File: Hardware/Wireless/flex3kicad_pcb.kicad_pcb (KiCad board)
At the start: 2 copper layers, 19 x 49.9 mm, 2 parts

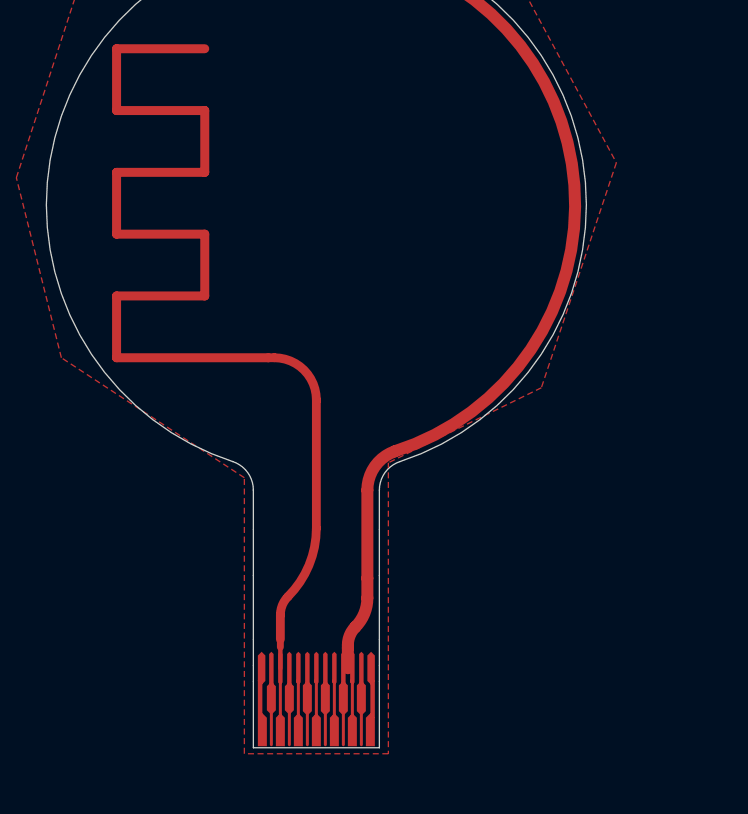
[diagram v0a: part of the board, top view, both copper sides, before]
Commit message: added status led
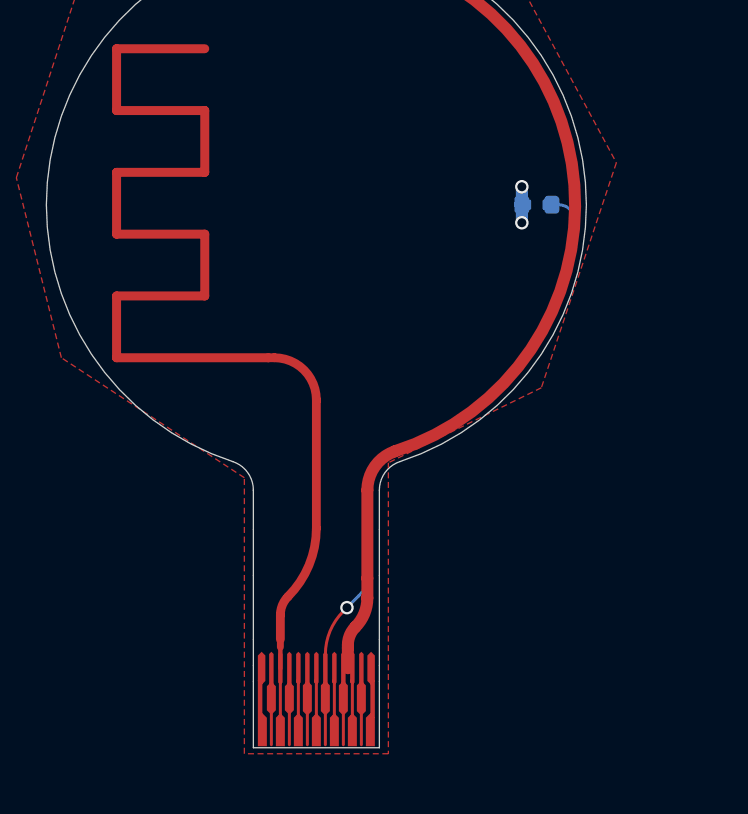
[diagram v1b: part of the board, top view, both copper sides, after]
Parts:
- added D1: BLUE, Library:0402, B.Cu at (185.2, 75.9)
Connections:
- REF** pad 8: (no net) -> led
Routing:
- net led: track 0.00 -> 7.54 mm, vias 0 -> 1
- net gnd: track 0.00 -> 1.20 mm, vias 0 -> 2

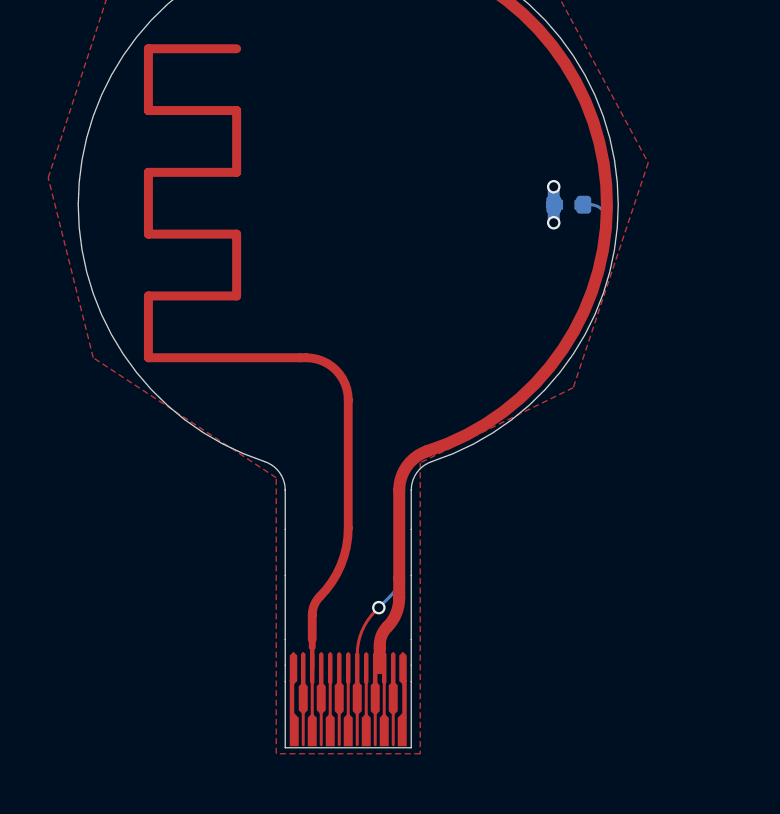
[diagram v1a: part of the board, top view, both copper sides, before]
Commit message: revolute production boards
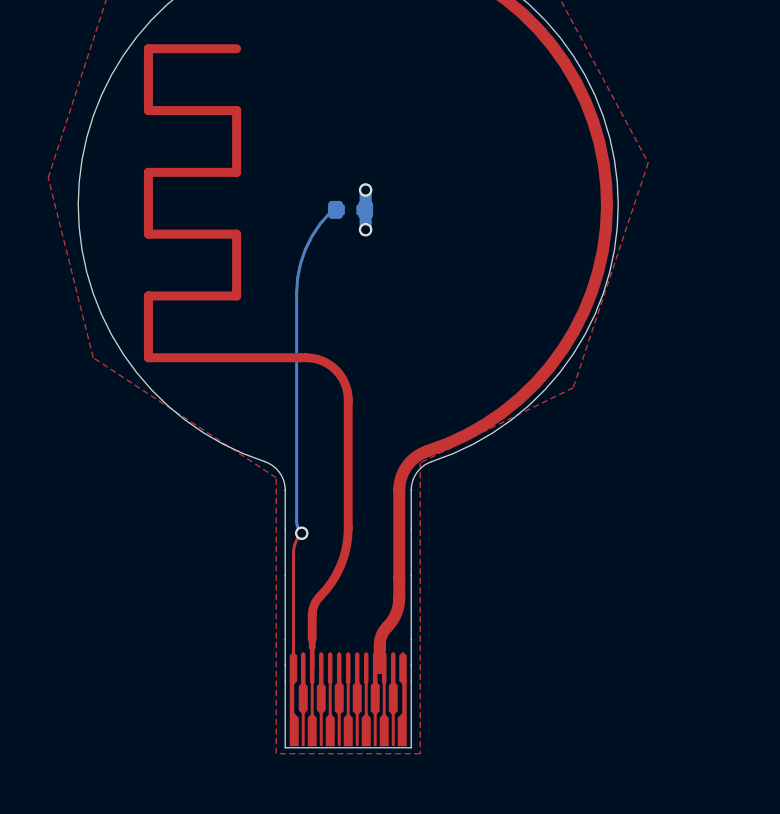
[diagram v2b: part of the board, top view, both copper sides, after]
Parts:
- moved D1 7.27 mm to (178.0, 76.1), turned to 0 degrees
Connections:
- REF** pad 1: gnd -> led
- REF** pad 8: led -> (no net)
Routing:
- net led: track 7.54 -> 15.6 mm

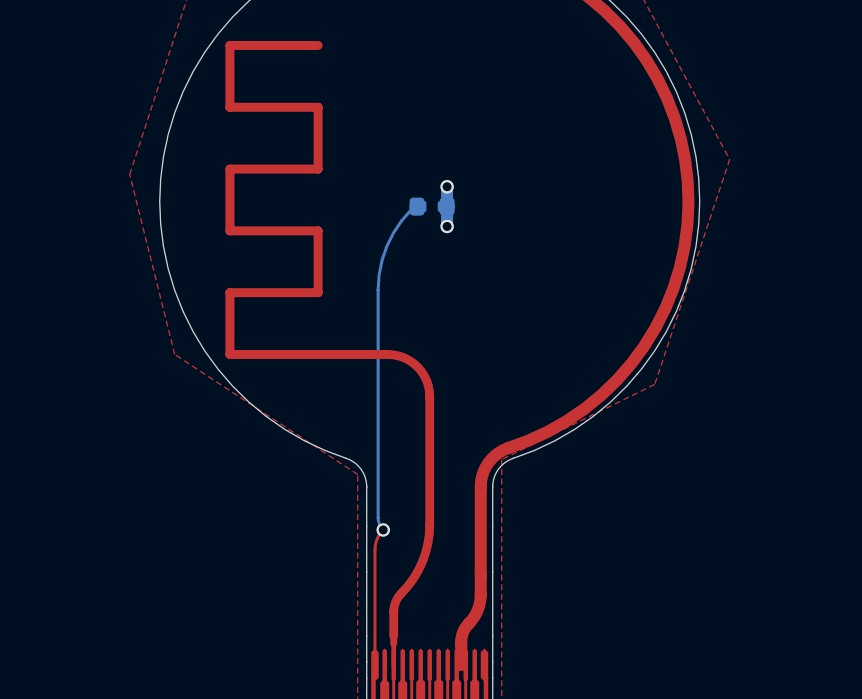
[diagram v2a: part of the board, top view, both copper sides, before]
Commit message: centered flex pcb, made pcb 1.6mm
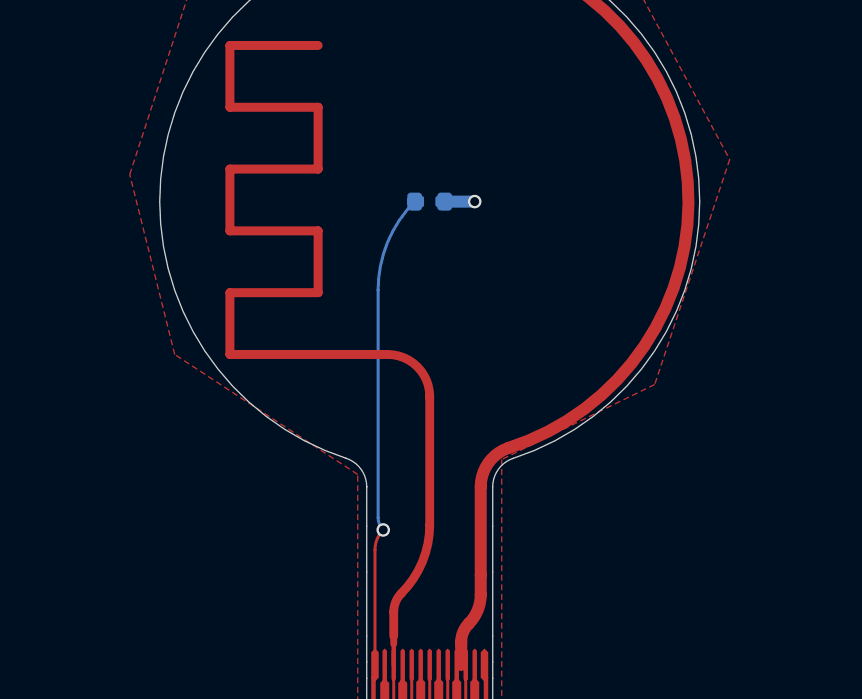
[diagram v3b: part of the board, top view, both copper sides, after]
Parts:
- moved D1 0.19 mm to (177.9, 75.9)
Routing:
- net gnd: track 1.32 -> 1.00 mm, vias 2 -> 1
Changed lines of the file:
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@@
 		(allow_soldermask_bridges_in_footprints no)
 		(aux_axis_origin 171 95)
-		(grid_origin 177.9791 76.0709)
+		(grid_origin 177.89999 75.903507)
 		(pcbplotparams
 			(layerselection 0x00410fc_ffffffff)
@@
 			(drillshape 0)
 			(scaleselection 1)
-			(outputdirectory "../../../../../../../../Desktop/RevoluteJanurary/Flex/")
+			(outputdirectory "../../../gerberflex/")
 		)
 	)
@@
 	(footprint "Library:0402"
 		(layer "B.Cu")
-		(at 177.9791 76.0709)
+		(at 177.89999 75.903507)
 		(property "Reference" "D1"
 			(at 0.040001 1.829998 180)
@@
 	)
 	(gr_arc
-		(start 175.499106 84.670778)
-		(mid 169.028778 76.0709)
-		(end 175.499106 67.471022)
+		(start 175.419996 84.503385)
+		(mid 168.949668 75.903507)
+		(end 175.419996 67.303629)
 		(stroke
 			(width 0.1)
@@
 		(layer "User.1")
 	)
-	(gr_arc
-		(start 175.698594 84.55781)
-		(mid 169.191364 76.134519)
-		(end 175.575958 67.617897)
+	(gr_line
+		(start 175.240886 62.24302)
+		(end 180.559114 62.24302)
+		(stroke
+			(width 1)
+			(type default)
+		)
+		(layer "User.1")
+	)
+	(gr_arc
+		(start 175.619484 84.390417)
+		(mid 169.112254 75.967126)
+		(end 175.496848 67.450504)
 		(stroke
 			(width 0.3)
@@
 	)
 	(gr_circle
-		(center 177.9791 76.0709)
-		(end 182.821644 76.083633)
+		(center 177.89999 75.903507)
+		(end 182.742534 75.91624)
 		(stroke
 			(width 7.5)
@@
 	)
 	(gr_line
-		(start 175.499106 84.670778)
-		(end 180.459094 84.670778)
+		(start 175.419996 84.503385)
+		(end 180.379984 84.503385)
 		(stroke
 			(width 0.1)
@@
 	)
 	(gr_arc
-		(start 180.278254 67.576361)
-		(mid 186.77911 76.015206)
-		(end 180.385585 84.535656)
+		(start 180.199144 67.408968)
+		(mid 186.700001 75.847814)
+		(end 180.306475 84.368263)
 		(stroke
 			(width 0.3)
@@
 	)
 	(gr_arc
-		(start 177.086246 84.556508)
-		(mid 169.446795 76.121011)
-		(end 176.986638 67.596364)
+		(start 177.007136 84.389115)
+		(mid 169.367685 75.953618)
+		(end 176.907528 67.428971)
 		(stroke
 			(width 0.3)
@@
 	)
 	(gr_arc
-		(start 178.871953 67.585291)
-		(mid 186.511404 76.020788)
-		(end 178.971561 84.545435)
+		(start 178.792843 67.417898)
+		(mid 186.432295 75.853396)
+		(end 178.892451 84.378042)
 		(stroke
 			(width 0.3)
@@
 	)
 	(gr_arc
-		(start 176.478076 84.562286)
-		(mid 169.356111 76.098314)
-		(end 176.424115 67.589229)
+		(start 176.398966 84.394893)
+		(mid 169.277 75.930921)
+		(end 176.345005 67.421836)
 		(stroke
 			(width 0.3)
@@
 	)
 	(gr_arc
-		(start 179.975777 67.585011)
-		(mid 186.696657 76.036228)
-		(end 180.043213 84.540637)
+		(start 179.896667 67.417618)
+		(mid 186.617549 75.868835)
+		(end 179.964103 84.373244)
 		(stroke
 			(width 0.3)
@@
 	)
 	(gr_line
-		(start 180.459094 67.471022)
-		(end 175.499106 67.471022)
+		(start 180.379984 67.303629)
+		(end 175.419996 67.303629)
 		(stroke
 			(width 0.1)
@@
 	)
 	(gr_arc
-		(start 179.480123 67.579513)
-		(mid 186.602089 76.043485)
-		(end 179.534084 84.55257)
+		(start 179.401013 67.41212)
+		(mid 186.522981 75.876093)
+		(end 179.454974 84.385177)
 		(stroke
 			(width 0.3)
@@
 	)
 	(gr_arc
-		(start 175.982422 84.556788)
-		(mid 169.261542 76.105571)
-		(end 175.914986 67.601162)
+		(start 175.903312 84.389395)
+		(mid 169.182432 75.938178)
+		(end 175.835876 67.433769)
 		(stroke
 			(width 0.3)
+			(type default)
+		)
+		(layer "User.1")
+	)
+	(gr_arc
+		(start 175.240886 62.24302)
+		(mid 177.9 44.631162)
+		(end 180.559114 62.24302)
+		(stroke
+			(width 1)
 			(type default)
 		)
@@
 	(gr_circle
 		(center 177.9 53.637833)
-		(end 187.399998 53.637833)
-		(stroke
-			(width 0)
-			(type solid)
-		)
-		(fill solid)
+		(end 182.138927 53.755212)
+		(stroke
+			(width 9)
+			(type default)
+		)
+		(fill none)
 		(layer "User.1")
 	)
 	(gr_arc
-		(start 180.459094 67.471022)
-		(mid 186.929422 76.0709)
-		(end 180.459094 84.670778)
+		(start 180.379984 67.303629)
+		(mid 186.850312 75.903507)
+		(end 180.379984 84.503385)
 		(stroke
 			(width 0.1)
@@
 	)
 	(via
-		(at 178.4791 76.732616)
+		(at 179.39999 75.903507)
 		(size 0.45)
 		(drill 0.3)
@@
 		(net 2)
 	)
-	(via
-		(at 178.4791 75.409182)
-		(size 0.45)
-		(drill 0.3)
-		(layers "F.Cu" "B.Cu")
-		(net 2)
-	)
 	(segment
-		(start 178.4791 76.070899)
-		(end 178.4791 75.409182)
-		(width 0.4)
-		(layer "B.Cu")
-		(net 2)
-	)
-	(segment
-		(start 178.4791 76.070899)
-		(end 178.4791 76.732616)
+		(start 178.39999 75.903506)
+		(end 179.399989 75.903506)
 		(width 0.4)
 		(layer "B.Cu")
@@
 	(segment
 		(start 176.179583 86.438577)
-		(end 176.179583 78.850784)
+		(end 176.179583 78.849831)
 		(width 0.1)
 		(layer "B.Cu")
@@
 	)
 	(arc
-		(start 176.179583 78.850784)
-		(mid 176.468171 77.399955)
-		(end 177.29 76.170001)
+		(start 176.179583 78.849831)
+		(mid 176.496756 77.255293)
+		(end 177.39999 75.903508)
 		(width 0.1)
 		(layer "B.Cu")
